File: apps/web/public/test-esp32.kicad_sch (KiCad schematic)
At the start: 9 parts, among them J1 USB_5V, SW1 EN_BTN, U1 ESP32-WROOM-32, U2 AMS1117-3.3

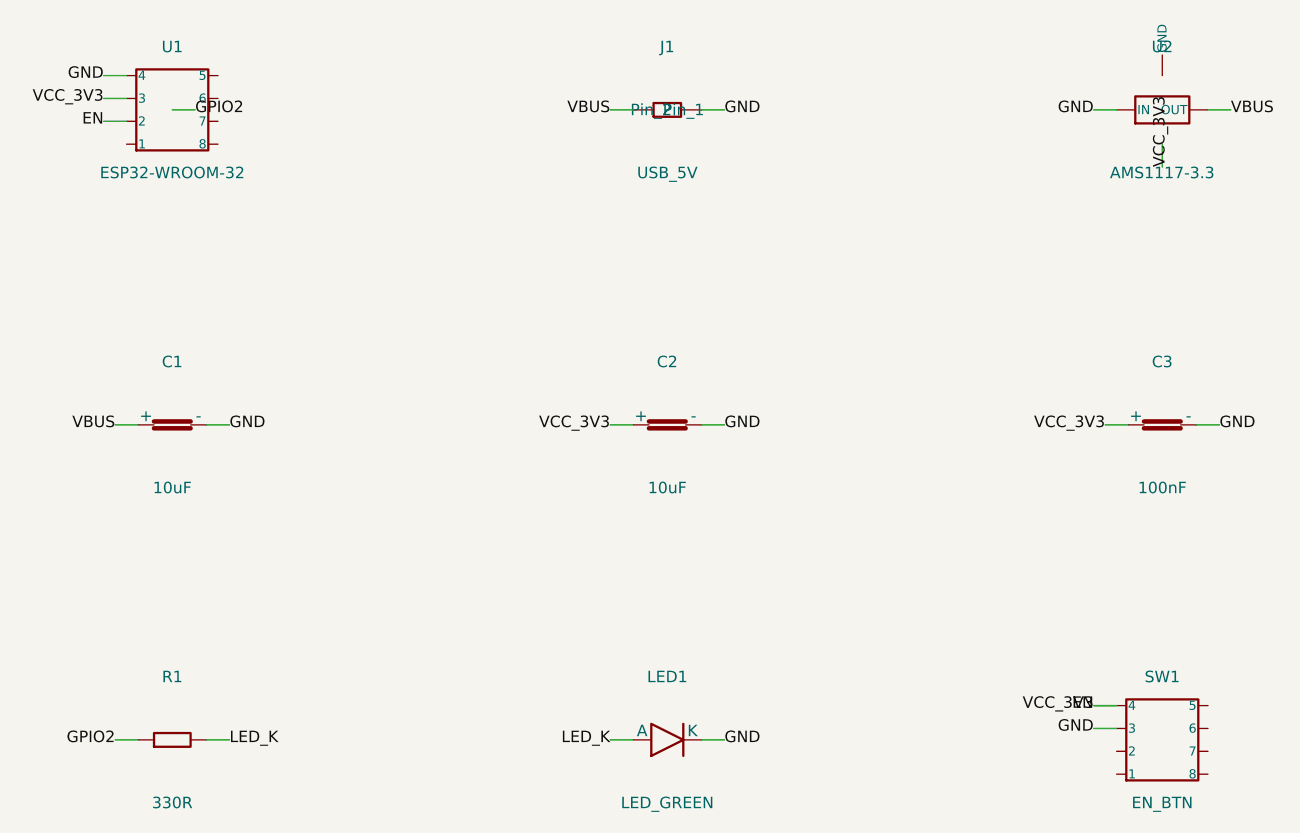
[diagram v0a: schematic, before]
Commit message: feat(schematic): pro upgrade — power symbols + title block
The previous fallback rendered GND/VCC nets as plain text labels, making
the schematic look like an MVP draft rather than a professional KiCad
deliverable. This brings it in line with industry-standard KiCad output.

Changes — circuit_synth.py:
- Added power:GND symbol (triangle) and power:VCC symbol (arrow+circle)
  inline in _INLINE_LIB_SYMBOLS so KiCanvas can render them natively.
- _is_power_net(name) classifier:
  GND nets:  GND, VSS, AGND, DGND, PGND, GROUND
  VCC nets:  VCC, VDD, VBUS, VBAT
  Positive rails: any net starting with '+' (e.g. +5V, +3V3, +12V).
- _power_lib_id(name): returns the correct power lib_id per net name.
- _generate_schematic_fallback: power nets now place a (symbol lib_id …)
  at the stub endpoint instead of a (label …). The Value property is
  overridden so the actual net name (e.g. '+3V3', 'VBUS') displays
  correctly even though +5V/VCC reuse the same VCC arrow shape.
- Title block filled:
    title   = 'Layrix — {primary IC value}'
    date    = ISO YYYY-MM-DD (today)
    rev     = '1.0'
    company = 'Layrix.ai'
- Helpers _today_iso() and _derive_title() added.

Tests — services/kicad/tests/test_circuit_synth_pro.py (NEW):
- 21 pytest tests across 3 classes (TestIsPowerNet, TestInlineLibSymbols,
  TestSchematicProGeneration) — TDD red->green cycle followed.
- Coverage: power-net classification, library symbol presence, title
  block fields, GND power-symbol substitution (no regression on signal
  net labels), VCC arrow on +5V/+3V3 rails.

Verification:
- pytest tests/test_circuit_synth_pro.py: 21/21 passing
- 3 test schematics regenerated via POST /circuit-synth/generate
- Visual check via Chrome DevTools on http://localhost:3333/test-cs.html:
  GND triangles on all 3 boards, VCC arrows on ESP32 (VCC_3V3/VBUS),
  VIN/VOUT/GPIO2 labels preserved on non-power nets.

docs/notefinal.md: STEP 2 'Validations réalisées' enriched with sprint
  'Schéma Pro' summary.
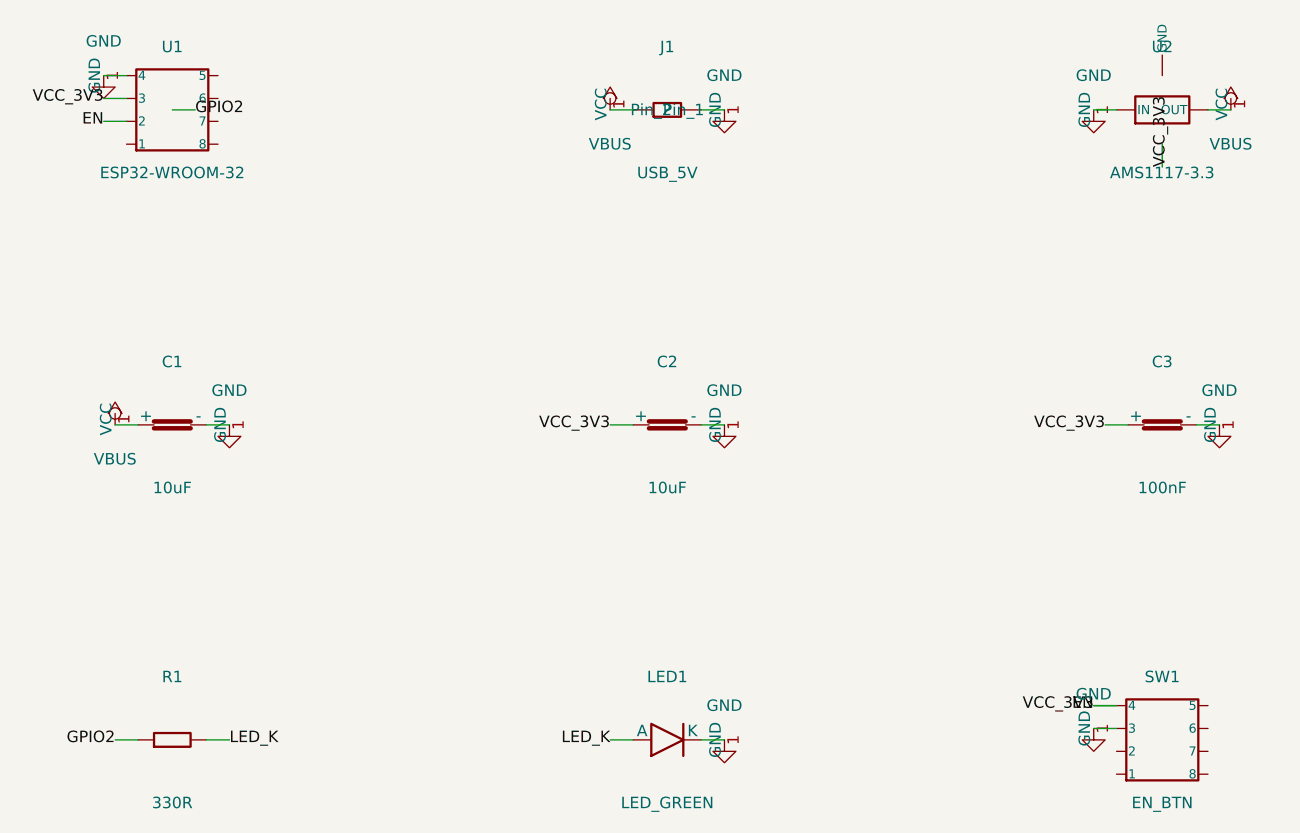
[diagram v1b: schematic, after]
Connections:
- net VBUS renamed VCC
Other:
- company: (none) -> Layrix.ai
- title: (none) -> Layrix — ESP32-WROOM-32
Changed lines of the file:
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@@
 (kicad_sch (version 20230121) (generator "layrix-circuit-synth")
   (paper "User" 206 172)
+  (title_block
+    (title "Layrix — ESP32-WROOM-32")
+    (date "2026-04-28")
+    (rev "1.0")
+    (company "Layrix.ai")
+  )
   (symbol (lib_id "Device:IC") (at 38 25 0) (unit 1) (in_bom yes) (on_board yes)
     (property "Reference" "U1" (at 38 18 0) (effects (font (size 1.27 1.27)) (justify center)))
@@
   )
   (wire (pts (xy 89.19 25.0) (xy 86.65 25.0)) (stroke (width 0.1524) (type default)))
-  (label "VBUS" (at 86.65 25.0 180) (effects (font (size 1.27 1.27))))
+  (symbol (lib_id "power:VCC") (at 86.65 25.0 0) (unit 1) (in_bom no) (on_board yes)
+    (property "Reference" "#PWR" (at 86.65 18.65 0) (effects (font (size 1.27 1.27)) hide))
+    (property "Value" "VBUS" (at 86.65 28.81 0) (effects (font (size 1.27 1.27))))
+  )
   (wire (pts (xy 153.08 25.0) (xy 155.62 25.0)) (stroke (width 0.1524) (type default)))
-  (label "VBUS" (at 155.62 25.0 0) (effects (font (size 1.27 1.27))))
+  (symbol (lib_id "power:VCC") (at 155.62 25.0 0) (unit 1) (in_bom no) (on_board yes)
+    (property "Reference" "#PWR" (at 155.62 18.65 0) (effects (font (size 1.27 1.27)) hide))
+    (property "Value" "VBUS" (at 155.62 28.81 0) (effects (font (size 1.27 1.27))))
+  )
   (wire (pts (xy 34.19 60.0) (xy 31.65 60.0)) (stroke (width 0.1524) (type default)))
-  (label "VBUS" (at 31.65 60.0 180) (effects (font (size 1.27 1.27))))
+  (symbol (lib_id "power:VCC") (at 31.65 60.0 0) (unit 1) (in_bom no) (on_board yes)
+    (property "Reference" "#PWR" (at 31.65 53.65 0) (effects (font (size 1.27 1.27)) hide))
+    (property "Value" "VBUS" (at 31.65 63.81 0) (effects (font (size 1.27 1.27))))
+  )
   (wire (pts (xy 148.0 28.81) (xy 148.0 31.35)) (stroke (width 0.1524) (type default)))
   (label "VCC_3V3" (at 148.0 31.35 90) (effects (font (size 1.27 1.27))))
@@
   (label "VCC_3V3" (at 140.38 91.19 180) (effects (font (size 1.27 1.27))))
   (wire (pts (xy 96.81 25.0) (xy 99.35 25.0)) (stroke (width 0.1524) (type default)))
-  (label "GND" (at 99.35 25.0 0) (effects (font (size 1.27 1.27))))
+  (symbol (lib_id "power:GND") (at 99.35 25.0 0) (unit 1) (in_bom no) (on_board yes)
+    (property "Reference" "#PWR" (at 99.35 18.65 0) (effects (font (size 1.27 1.27)) hide))
+    (property "Value" "GND" (at 99.35 21.19 0) (effects (font (size 1.27 1.27))))
+  )
   (wire (pts (xy 142.92 25.0) (xy 140.38 25.0)) (stroke (width 0.1524) (type default)))
-  (label "GND" (at 140.38 25.0 180) (effects (font (size 1.27 1.27))))
+  (symbol (lib_id "power:GND") (at 140.38 25.0 0) (unit 1) (in_bom no) (on_board yes)
+    (property "Reference" "#PWR" (at 140.38 18.65 0) (effects (font (size 1.27 1.27)) hide))
+    (property "Value" "GND" (at 140.38 21.19 0) (effects (font (size 1.27 1.27))))
+  )
   (wire (pts (xy 41.81 60.0) (xy 44.35 60.0)) (stroke (width 0.1524) (type default)))
-  (label "GND" (at 44.35 60.0 0) (effects (font (size 1.27 1.27))))
+  (symbol (lib_id "power:GND") (at 44.35 60.0 0) (unit 1) (in_bom no) (on_board yes)
+    (property "Reference" "#PWR" (at 44.35 53.65 0) (effects (font (size 1.27 1.27)) hide))
+    (property "Value" "GND" (at 44.35 56.19 0) (effects (font (size 1.27 1.27))))
+  )
   (wire (pts (xy 96.81 60.0) (xy 99.35 60.0)) (stroke (width 0.1524) (type default)))
-  (label "GND" (at 99.35 60.0 0) (effects (font (size 1.27 1.27))))
+  (symbol (lib_id "power:GND") (at 99.35 60.0 0) (unit 1) (in_bom no) (on_board yes)
+    (property "Reference" "#PWR" (at 99.35 53.65 0) (effects (font (size 1.27 1.27)) hide))
+    (property "Value" "GND" (at 99.35 56.19 0) (effects (font (size 1.27 1.27))))
+  )
   (wire (pts (xy 151.81 60.0) (xy 154.35 60.0)) (stroke (width 0.1524) (type default)))
-  (label "GND" (at 154.35 60.0 0) (effects (font (size 1.27 1.27))))
+  (symbol (lib_id "power:GND") (at 154.35 60.0 0) (unit 1) (in_bom no) (on_board yes)
+    (property "Reference" "#PWR" (at 154.35 53.65 0) (effects (font (size 1.27 1.27)) hide))
+    (property "Value" "GND" (at 154.35 56.19 0) (effects (font (size 1.27 1.27))))
+  )
   (wire (pts (xy 32.92 21.19) (xy 30.38 21.19)) (stroke (width 0.1524) (type default)))
-  (label "GND" (at 30.38 21.19 180) (effects (font (size 1.27 1.27))))
+  (symbol (lib_id "power:GND") (at 30.38 21.19 0) (unit 1) (in_bom no) (on_board yes)
+    (property "Reference" "#PWR" (at 30.38 14.840000000000002 0) (effects (font (size 1.27 1.27)) hide))
+    (property "Value" "GND" (at 30.38 17.380000000000003 0) (effects (font (size 1.27 1.27))))
+  )
   (wire (pts (xy 96.81 95.0) (xy 99.35 95.0)) (stroke (width 0.1524) (type default)))
-  (label "GND" (at 99.35 95.0 0) (effects (font (size 1.27 1.27))))
+  (symbol (lib_id "power:GND") (at 99.35 95.0 0) (unit 1) (in_bom no) (on_board yes)
+    (property "Reference" "#PWR" (at 99.35 88.65 0) (effects (font (size 1.27 1.27)) hide))
+    (property "Value" "GND" (at 99.35 91.19 0) (effects (font (size 1.27 1.27))))
+  )
   (wire (pts (xy 142.92 93.73) (xy 140.38 93.73)) (stroke (width 0.1524) (type default)))
-  (label "GND" (at 140.38 93.73 180) (effects (font (size 1.27 1.27))))
+  (symbol (lib_id "power:GND") (at 140.38 93.73 0) (unit 1) (in_bom no) (on_board yes)
+    (property "Reference" "#PWR" (at 140.38 87.38000000000001 0) (effects (font (size 1.27 1.27)) hide))
+    (property "Value" "GND" (at 140.38 89.92 0) (effects (font (size 1.27 1.27))))
+  )
   (wire (pts (xy 32.92 26.27) (xy 30.38 26.27)) (stroke (width 0.1524) (type default)))
   (label "EN" (at 30.38 26.27 180) (effects (font (size 1.27 1.27))))
